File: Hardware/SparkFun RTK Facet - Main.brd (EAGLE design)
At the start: 60 x 40 mm, 125 parts, among them J1 QWIIC_RIGHT_ANGLE, J15 FPC_12_0.5MM2, J18 FPC_12_0.5MM2, J2 U.FL, J8 FPC_12_0.5MM2, Q2 MBT3904DW1T1, Q3 SIL2308, U1 74HC4052D, U10 MCP73833, U12 AP2112K-3.3, U2 3.3V, U3 U-BLOX_ZED-F9P, U4 ADP160, U5 ESP-WROOM-32NARROW, U6 CH340C, U7 MAX17048, U8 USB251XB, Y1 24MHz

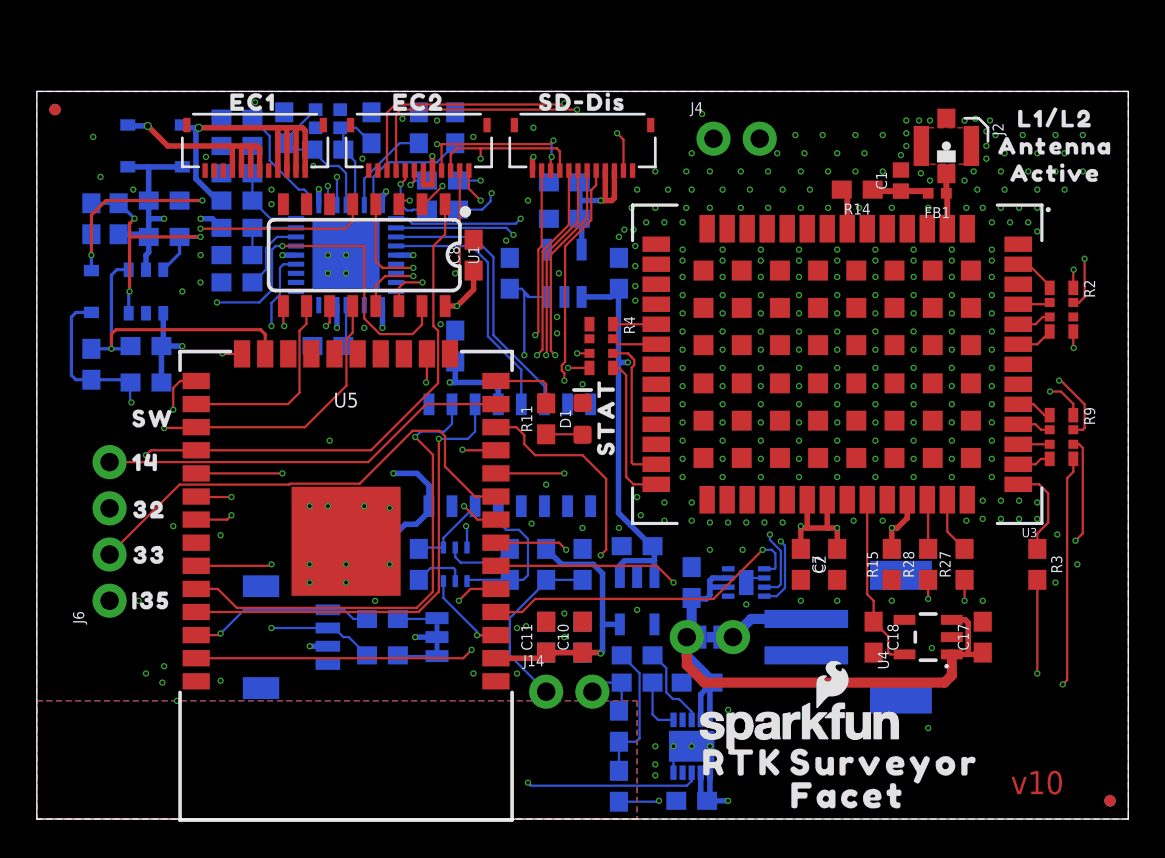
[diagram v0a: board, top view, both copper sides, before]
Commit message: Move display connector to side so overlay connector can be center. Notch PCBs. Add dummy PCB height. Add dummy retention plate.
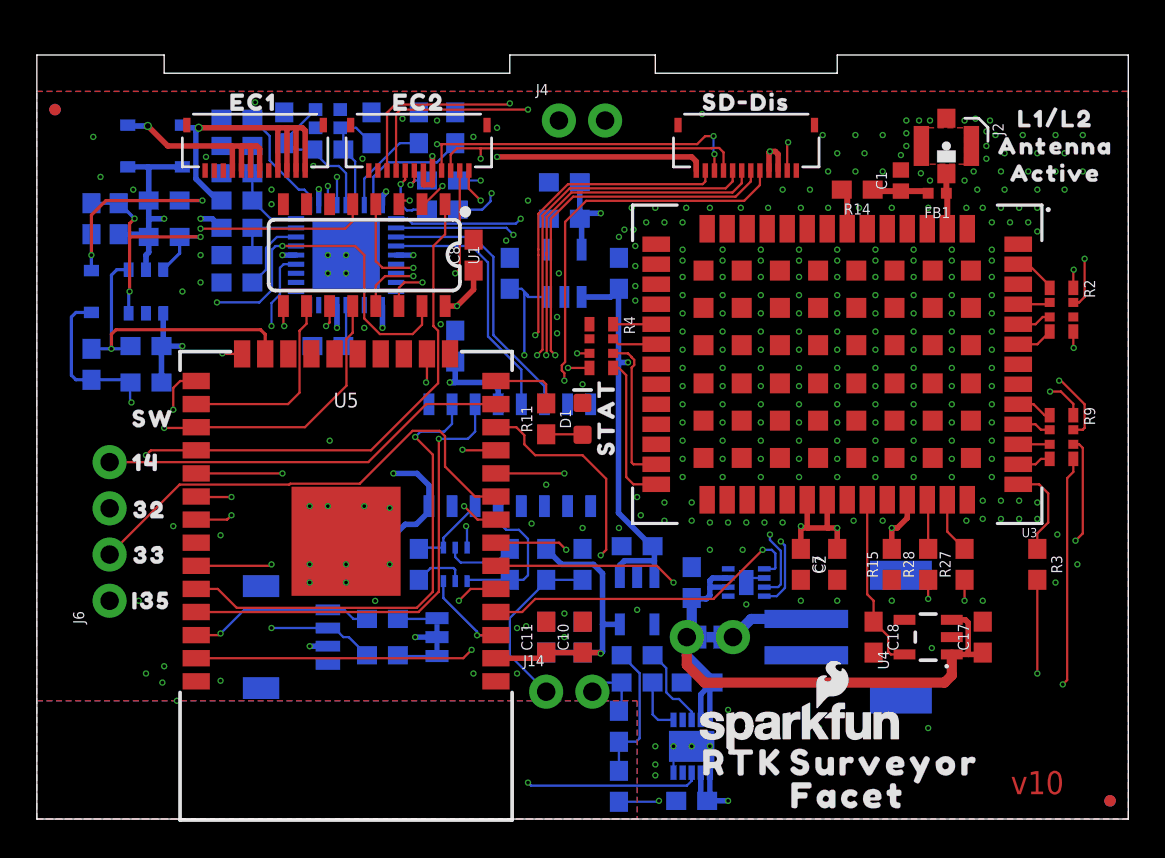
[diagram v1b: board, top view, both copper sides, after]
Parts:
- moved J8 9.00 mm to (39.0, 37.0)
- moved U$4 9.00 mm to (39.0, 39.4)
- moved J4 8.56 mm to (28.7, 38.4)
- moved U$10 8.56 mm to (31.3, 35.9)
- moved U$6 8.55 mm to (28.7, 35.7)
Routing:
- net ESP_21/SDA: track 118.6 -> 127.7 mm
- net ESP_23/SD_COPI: track 47.6 -> 56.6 mm
- net ESP_18/SD_SCK: track 37.5 -> 46.4 mm
- net ESP_25/SD_!CS!: track 21.3 -> 30.1 mm
- net V_USB: track 41.8 -> 50.6 mm
- net ESP_19/SD_CIPO: track 39.0 -> 47.8 mm
- net ESP_22/SCL: track 134.3 -> 143.0 mm
- net POWER_BTN: track 49.8 -> 58.4 mm
- net CHG_LED: track 43.9 -> 52.0 mm
- net ZED-TXO2: track 28.9 -> 27.2 mm
- net ZED-RXI2: track 27.2 -> 25.7 mm
- net 3.3V: track 47.0 -> 45.5 mm, vias 17 -> 18
- net ZED_EXTINT: track 75.8 -> 75.2 mm
- net ZED_PPS_STAT: track 58.1 -> 57.5 mm
- net GND: vias 290 -> 275
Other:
- board size 60 x 40 mm -> 60 x 42 mm

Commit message: Adjust top edges for alignment.
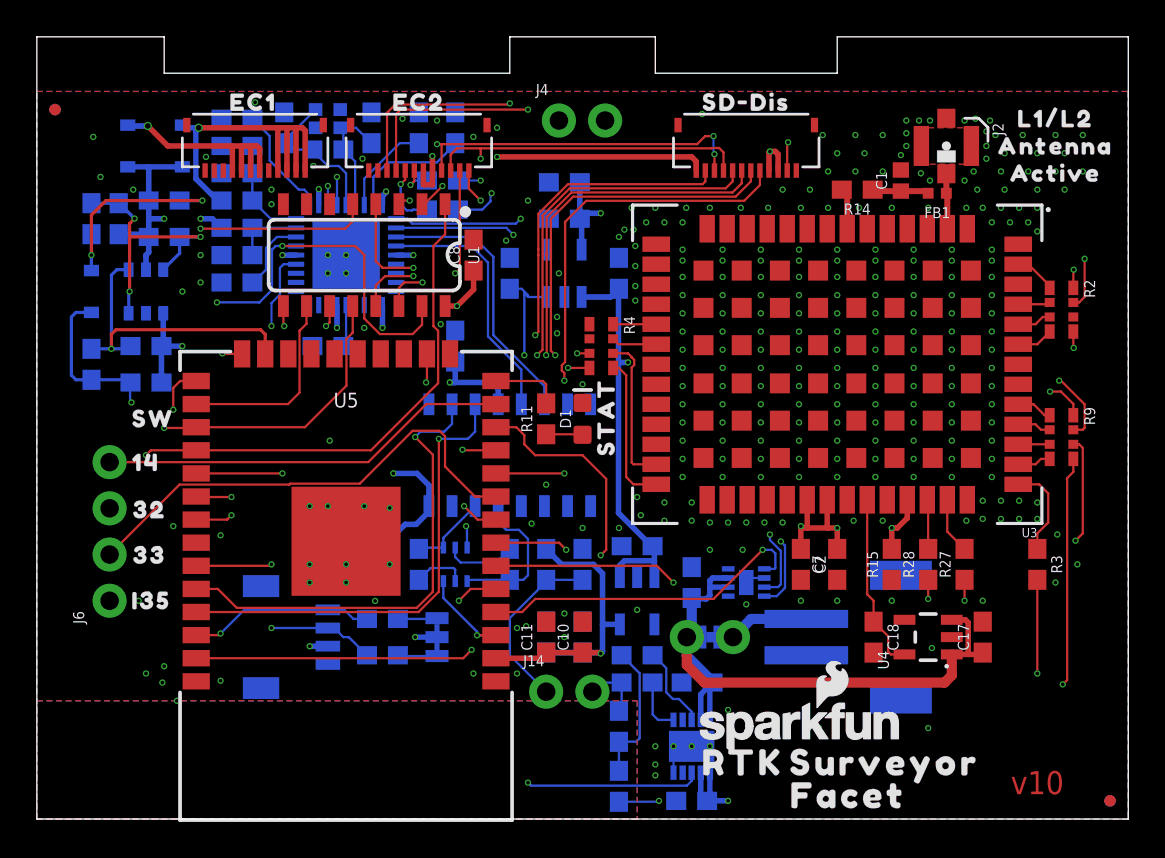
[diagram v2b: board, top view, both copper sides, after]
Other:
- board size 60 x 42 mm -> 60 x 43 mm
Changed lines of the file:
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@@
 <layer number="1" name="Top/Horz" color="4" fill="1" visible="yes" active="yes"/>
 <layer number="2" name="GND/Horz" color="1" fill="3" visible="yes" active="yes"/>
-<layer number="15" name="3.3V/Vert" color="4" fill="6" visible="yes" active="yes"/>
+<layer number="15" name="3.3V/Vert" color="4" fill="6" visible="no" active="yes"/>
 <layer number="16" name="Bottom/Vert" color="1" fill="1" visible="yes" active="yes"/>
 <layer number="17" name="Pads" color="2" fill="1" visible="yes" active="yes"/>
@@
 <text x="41.1" y="7.6" size="1.778" layer="22" font="vector" ratio="15" rot="MR180" align="center">-</text>
 <text x="41.1" y="12.3" size="1.778" layer="22" font="vector" ratio="15" rot="MR180" align="center">+</text>
-<wire x1="60" y1="42" x2="60" y2="0" width="0.05" layer="20"/>
+<wire x1="60" y1="43" x2="60" y2="0" width="0.05" layer="20"/>
 <wire x1="60" y1="0" x2="0" y2="0" width="0.05" layer="20"/>
-<wire x1="0" y1="0" x2="0" y2="42" width="0.05" layer="20"/>
+<wire x1="0" y1="0" x2="0" y2="43" width="0.05" layer="20"/>
 <rectangle x1="-0.96" y1="0" x2="1.04" y2="40" layer="39"/>
 <rectangle x1="57.04" y1="0" x2="59.04" y2="40" layer="39"/>
@@
 <rectangle x1="57.04" y1="0" x2="59.04" y2="40" layer="40"/>
 <wire x1="30" y1="43" x2="30" y2="-2" width="0.127" layer="51"/>
-<wire x1="0" y1="42" x2="7" y2="42" width="0.05" layer="20"/>
-<wire x1="7" y1="42" x2="7" y2="41" width="0.05" layer="20"/>
+<wire x1="0" y1="43" x2="7" y2="43" width="0.05" layer="20"/>
+<wire x1="7" y1="43" x2="7" y2="41" width="0.05" layer="20"/>
 <wire x1="7" y1="41" x2="26" y2="41" width="0.05" layer="20"/>
-<wire x1="26" y1="41" x2="26" y2="42" width="0.05" layer="20"/>
-<wire x1="26" y1="42" x2="34" y2="42" width="0.05" layer="20"/>
-<wire x1="34" y1="42" x2="34" y2="41" width="0.05" layer="20"/>
+<wire x1="26" y1="41" x2="26" y2="43" width="0.05" layer="20"/>
+<wire x1="26" y1="43" x2="34" y2="43" width="0.05" layer="20"/>
+<wire x1="34" y1="43" x2="34" y2="41" width="0.05" layer="20"/>
 <wire x1="34" y1="41" x2="44" y2="41" width="0.05" layer="20"/>
-<wire x1="44" y1="41" x2="44" y2="42" width="0.05" layer="20"/>
-<wire x1="44" y1="42" x2="60" y2="42" width="0.05" layer="20"/>
+<wire x1="44" y1="41" x2="44" y2="43" width="0.05" layer="20"/>
+<wire x1="44" y1="43" x2="60" y2="43" width="0.05" layer="20"/>
 </plain>
 <attributes>
@@
 <wire x1="36.8841" y1="39.0714" x2="36.5714" y2="38.7587" width="0.127" layer="15"/>
 <wire x1="56.2" y1="39.0714" x2="36.8841" y2="39.0714" width="0.127" layer="15"/>
-<wire x1="36.5714" y1="38.7587" x2="31.5987" y2="38.7587" width="0.127" layer="2"/>
-<wire x1="31.5987" y1="38.7587" x2="31.240003125" y2="38.400003125" width="0.127" layer="2"/>
+<wire x1="36.5714" y1="38.7587" x2="31.7" y2="38.7587" width="0.127" layer="2"/>
 <wire x1="22" y1="38.4" x2="23.3" y2="39.7" width="0.127" layer="2"/>
+<wire x1="23.3" y1="39.7" x2="29.94" y2="39.7" width="0.127" layer="2"/>
 <wire x1="29.94" y1="39.7" x2="31.24" y2="38.4" width="0.127" layer="2"/>
-<wire x1="23.3" y1="39.7" x2="29.94" y2="39.7" width="0.127" layer="2"/>
+<wire x1="31.24" y1="38.4" x2="31.5987" y2="38.7587" width="0.127" layer="2"/>
+<wire x1="31.5987" y1="38.7587" x2="31.7" y2="38.7587" width="0.127" layer="2"/>
 </signal>
 <signal name="N$2">

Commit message: Update PROD ID on 12 pin connector. Add gerbers for v10.
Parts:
- J15, J18, J8: value FPC_12_0.5MM2 -> FPC_12_0.5MM_BACKFLIP; device RTK Facet:FPC_12_FLIP_DOUBLESIDED_2 -> RTK Facet:FPC_12_DOUBLESIDED_BACKFLIP
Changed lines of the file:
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@@
 <setting verticaltext="up"/>
 </settings>
-<grid distance="1" unitdist="mm" unit="mm" style="lines" multiple="1" display="yes" altdistance="0.1" altunitdist="mm" altunit="mm"/>
+<grid distance="0.05" unitdist="inch" unit="inch" style="lines" multiple="1" display="yes" altdistance="0.005" altunitdist="inch" altunit="inch"/>
 <layers>
 <layer number="1" name="Top/Horz" color="4" fill="1" visible="yes" active="yes"/>
-<layer number="2" name="GND/Horz" color="1" fill="3" visible="yes" active="yes"/>
+<layer number="2" name="GND/Horz" color="1" fill="3" visible="no" active="yes"/>
 <layer number="15" name="3.3V/Vert" color="4" fill="6" visible="no" active="yes"/>
 <layer number="16" name="Bottom/Vert" color="1" fill="1" visible="yes" active="yes"/>
@@
 <layer number="47" name="Measures" color="7" fill="1" visible="no" active="yes"/>
 <layer number="48" name="Document" color="7" fill="1" visible="no" active="yes"/>
-<layer number="49" name="Reference" color="7" fill="1" visible="yes" active="yes"/>
+<layer number="49" name="Reference" color="7" fill="1" visible="no" active="yes"/>
 <layer number="50" name="dxf" color="7" fill="1" visible="no" active="yes"/>
 <layer number="51" name="tDocu" color="6" fill="1" visible="yes" active="yes"/>
@@
 <attribute name="VALUE" x="24.772" y="31" size="0.6096" layer="27" font="vector" ratio="20" rot="R90" align="top-center"/>
 </element>
-<element name="J15" library="RTK Facet" package="FPC_12_FLIP_DOUBLESIDED_2" value="FPC_12_0.5MM2" x="12" y="37" smashed="yes" rot="R180"/>
-<element name="J18" library="RTK Facet" package="FPC_12_FLIP_DOUBLESIDED_2" value="FPC_12_0.5MM2" x="21" y="37" smashed="yes" rot="R180"/>
+<element name="J15" library="RTK Facet" package="FPC_12_DOUBLESIDED_BACKFLIP" value="FPC_12_0.5MM_BACKFLIP" x="12" y="37" smashed="yes" rot="R180">
+<attribute name="PROD_ID" value="CONN-15766" x="12" y="37" size="1.778" layer="27" rot="R180" display="off"/>
+</element>
+<element name="J18" library="RTK Facet" package="FPC_12_DOUBLESIDED_BACKFLIP" value="FPC_12_0.5MM_BACKFLIP" x="21" y="37" smashed="yes" rot="R180">
+<attribute name="PROD_ID" value="CONN-15766" x="21" y="37" size="1.778" layer="27" rot="R180" display="off"/>
+</element>
 <element name="U$8" library="output" package="EC10" value="" x="11.9" y="39.4" smashed="yes"/>
 <element name="U$3" library="output" package="EC21" value="" x="21" y="39.4" smashed="yes"/>
@@
 <attribute name="VALUE" x="11" y="36.238" size="0.6096" layer="28" font="vector" ratio="20" rot="MR0" align="top-center"/>
 </element>
-<element name="J8" library="RTK Facet" package="FPC_12_FLIP_DOUBLESIDED_2" value="FPC_12_0.5MM2" x="39" y="37" smashed="yes" rot="R180"/>
+<element name="J8" library="RTK Facet" package="FPC_12_DOUBLESIDED_BACKFLIP" value="FPC_12_0.5MM_BACKFLIP" x="39" y="37" smashed="yes" rot="R180">
+<attribute name="PROD_ID" value="CONN-15766" x="39" y="37" size="1.778" layer="27" rot="R180" display="off"/>
+</element>
 </elements>
 <signals>

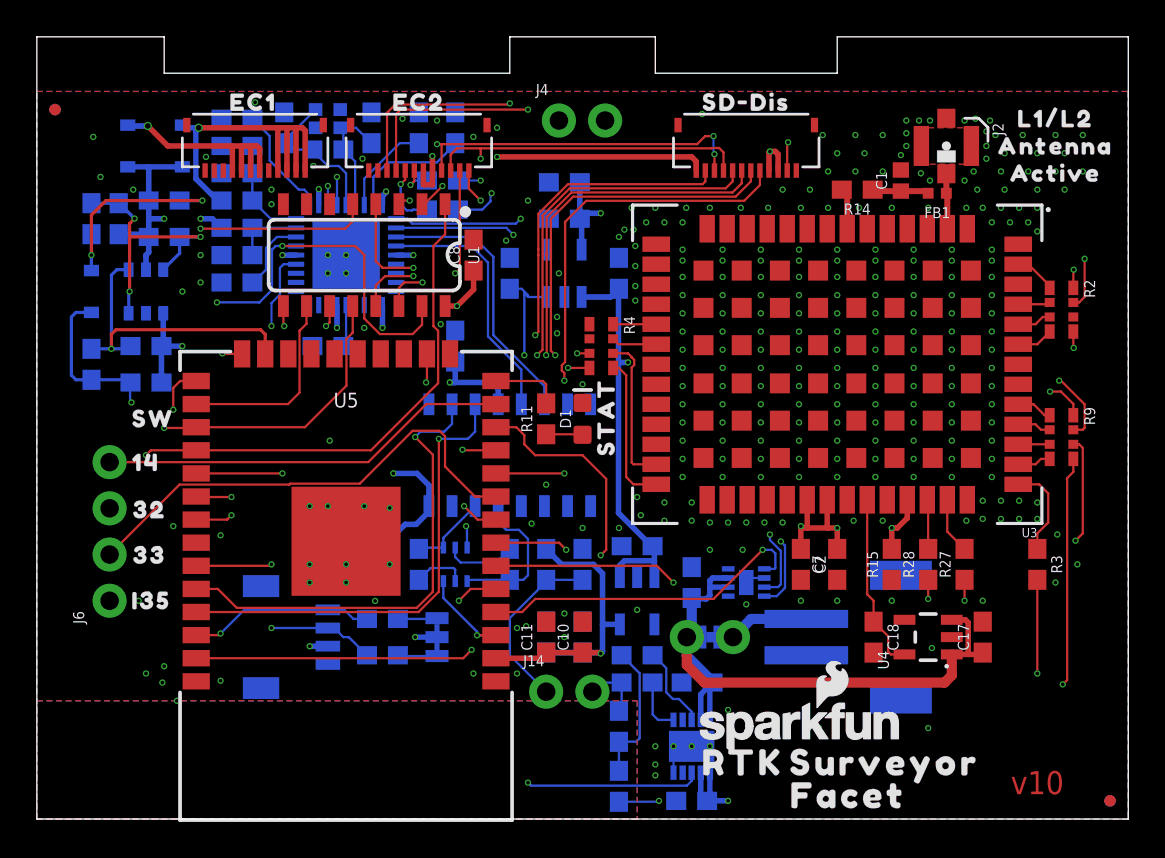
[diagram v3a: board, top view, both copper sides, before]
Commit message: Move external connectors to button control. Add radio connector. Move ESP32 to VOUT. Move USB to VOUT. Remove USB from I2C.
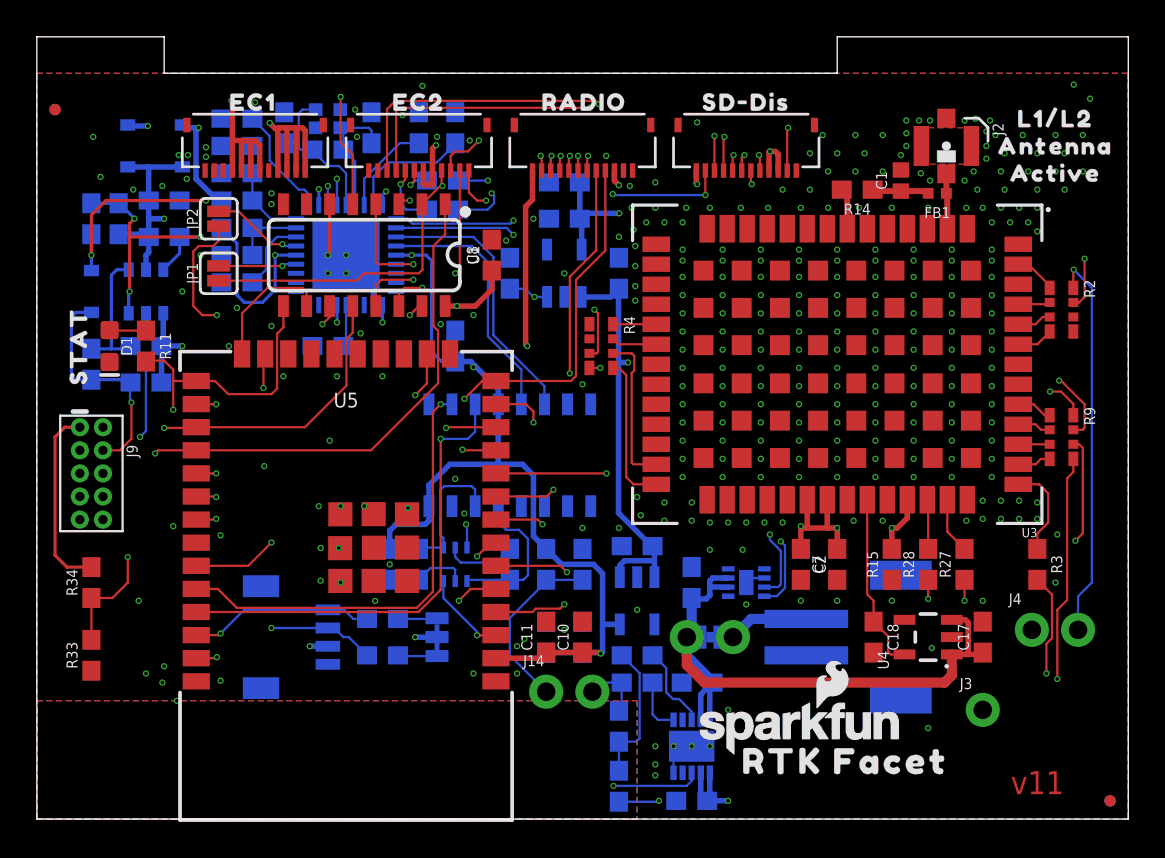
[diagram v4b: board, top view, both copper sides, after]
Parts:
- removed J6: (no value), SparkFun-Connectors:1X04_NO_SILK
- removed U$15, U$19: (no value), output:RTK0
- removed U$16, U$18: (no value), output:SURVEYOR1
- removed U$17: (no value), output:FACET2
- removed U$20: (no value), output:140
- removed U$21: (no value), output:321
- removed U$22: (no value), output:332
- removed U$23: (no value), output:I353
- added J10: (no value), RTK Facet:FPC_12_DOUBLESIDED_BACKFLIP
- added J3: (no value), SparkFun-Connectors:1X01_NO_SILK
- added J9: CORTEX_JTAG_DEBUG_PTH, SparkFun-Connectors:2X5-PTH-1.27MM
- added JP1, JP2: (no value), SparkFun-Jumpers:SMT-JUMPER_2_NO_SILK
- added R33, R34: 10k, SparkFun-Resistors:0603
- added U$11: (no value), output:RTK_FACET0
- added U$12: (no value), output:RADIO0
- J15, J18, J8: value FPC_12_0.5MM_BACKFLIP -> (none)
- U$13: device output:SW0 -> output:RTK_FACET0
- U$14: device output:FACET2 -> output:#GND#1
- U4: value ADP160 -> STLQ015
- U5: value ESP-WROOM-32NARROW -> ESP-WROOM-3232D-NARROW; device SparkFun-RF:ESP-WROOM-32-NARROW -> SparkFun-RF:ESP-WROOM-32D-NARROW
- moved U$6 38.2 mm to (54.7, 7.70)
- moved J4 38.2 mm to (54.7, 10.4)
- moved U$10 38.2 mm to (57.3, 7.90)
- moved U$13 35.3 mm to (41.5, 26.2), flipped to the bottom
- moved U$24 29.3 mm to (2.30, 26.0)
- moved D1 26.3 mm to (4.00, 26.0), turned to 270 degrees
- moved R11 22.4 mm to (6.00, 26.0), turned to 270 degrees
- moved U$14 12.2 mm to (52.0, 11.0), flipped to the bottom, turned to 270 degrees
- moved U$30 7.00 mm to (13.5, 14.6)
- moved LOGO1 4.69 mm to (51.0, 2.00)
- moved C8 1.00 mm to (25.0, 31.0)
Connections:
- removed net ESP_0/BOOT: Q2.6, U5.25
- removed net ESP_12/STAT_LED: R11.2, U5.14
- removed net ESP_13/POWER_CTRL: D4.A, R22.1, R24.2, U5.16
- removed net ESP_14: J6.4, U5.13
- removed net ESP_15/FAST_OFF: C20.2, Q3.G1, R24.1, U5.23
- removed net ESP_2/PERIPHERAL_POWER: R1.2, U12.3, U5.24
- removed net ESP_27/ZED_!RESET!: R2.P5, U5.12
- removed net ESP_32: J6.3, U5.8
- removed net ESP_33: J6.2, U5.9
- removed net ESP_36/BATT_ALRT: U5.4, U7.5
- removed net ESP_4/MUX_A: U1.10, U5.26
- removed net ESP_5/MUX_B: U1.9, U5.29
- removed net ESP_I34/ZED_TX_READY: R9.P8, U5.6
- removed net ESP_I35: J6.1, U5.7
- new net ESP_0/BOOT/STAT_LED/MUX_B: Q2.6, R11.2, U1.9, U5.25
- new net ESP_12/MTDI/RADIO_NI: J10.4, J9.8, U5.14
- new net ESP_13/POWER_CTRL/MTCK: D4.A, J9.4, R22.1, R24.2, U5.16
- new net ESP_14/PERIPHERAL_POWER/MTMS: J9.2, R1.2, U12.3, U5.13
- new net ESP_15/MTDO/RADIO_!RESET!: J10.5, J9.6, U5.23
- new net ESP_2/MUX_A: U1.10, U5.24
- new net ESP_27/FAST_OFF: C20.2, Q3.G1, R24.1, U5.12
- new net ESP_32/RADIO_TXO: J10.11, U5.8
- new net ESP_33/RADIO_RXI: J10.10, U5.9
- new net ESP_4/RADIO_PWR_ON: J10.6, U5.26
- new net ESP_5/RADIO_CTSI: J10.8, U5.29
- new net ESP_I34/RADIO_INT: J10.7, U5.6
- new net ESP_I35/DEVICE_SENSE: R33.2, R34.1, U5.7
- new net ESP_I36/RADIO_RTSO: J10.9, U5.4
- new net N$21: JP1.2, U8.22
- new net N$23: JP2.2, U8.24
- new net ZED_!RESET!: R2.P5
- new net ZED_TX_READY: R9.P8
- net 3.3V: now also J10.3; no longer C13.1, C14.1, R18.2, U6.16, U6.4, U8.10, U8.15, U8.23, U8.29, U8.36, U8.5
- net ESP32_EN: now also J9.10
- net ESP_21/SDA: now also JP1.1; no longer U8.22
- net ESP_22/SCL: now also JP2.1; no longer U8.24
- net ESP_3V3: now also C13.1, C14.1, J9.1, R18.2, R34.2, U6.16, U6.4, U8.10, U8.15, U8.23, U8.29, U8.36, U8.5
- net GND: now also J10.1, J10.2, J3.1, J9.3, J9.5, J9.7, J9.9, R33.1, U5.GND1, U5.GNDT1, U5.GNDT2, U5.GNDT3, U5.GNDT4, U5.GNDT5, U5.GNDT6, U5.GNDT7, U5.GNDT8; no longer U5.GND
- net VOUT: now also J10.12, J15.6, J15.7, J15.8, J15.9
- net V_BATT: no longer J15.6, J15.7, J15.8, J15.9
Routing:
- net ESP_3V3: track 18.0 -> 118.6 mm, vias 1 -> 11
- net ESP_27/ZED_!RESET!: track 51.4 -> 0.00 mm, vias 3 -> 0
- net ESP_15/MTDO/RADIO_!RESET!: track 0.00 -> 44.2 mm, vias 0 -> 3
- net ESP_I34/ZED_TX_READY: track 43.9 -> 0.00 mm, vias 3 -> 0
- net ESP_12/MTDI/RADIO_NI: track 0.00 -> 43.0 mm, vias 0 -> 2
- net ESP_5/RADIO_CTSI: track 0.00 -> 41.8 mm, vias 0 -> 3
- net ESP_0/BOOT/STAT_LED/MUX_B: track 0.00 -> 38.6 mm, vias 0 -> 3
- net ESP_4/RADIO_PWR_ON: track 0.00 -> 38.4 mm, vias 0 -> 3
- net ESP_14/PERIPHERAL_POWER/MTMS: track 0.00 -> 35.8 mm, vias 0 -> 2
- net VOUT: track 52.2 -> 85.8 mm, vias 2 -> 5
- net ESP_27/FAST_OFF: track 0.00 -> 32.6 mm, vias 0 -> 2
- net ESP_13/POWER_CTRL/MTCK: track 0.00 -> 31.1 mm, vias 0 -> 2
- net ESP_I35: track 30.3 -> 0.00 mm, vias 1 -> 0
- net ESP_I36/RADIO_RTSO: track 0.00 -> 29.6 mm, vias 0 -> 2
- net ESP_I34/RADIO_INT: track 0.00 -> 28.0 mm, vias 0 -> 2
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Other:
- outline, holes or cut-outs redrawn
- board text added: "v11"
- board text removed: "v10"
